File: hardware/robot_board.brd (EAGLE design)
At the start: 95.2 x 76.1 mm, 147 parts, among them J1 POWER_JACKPTH, Q1 DMP2035U, Q2 DMP2035U, Q3 DMP2035U-7, Q4 DMP2035U-7, U1 FT232RL-BASICSSOP, U11 LM393, U12 LM393, U16 LM393, U17 ATMEGA325PA, U2 SIA907EDJT, U3 MIC5219, U4 HC_05, U5 SIA907EDJT, U6 SIA907EDJT, U7 TLV70233, Y1 16MHz

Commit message: updated routing
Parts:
- removed D24: POWER, SparkFun-LED:LED-1206
- added C8: .1uF, resistor:C1206
- added C9: 1uF, resistor:C1206
- added D34: POWER, SparkFun-LED:LED-1206
- added R63: 1K, resistor:R1206
- added U$2: POT, r_cubed:POT
- D23: value 2.1V -> 2.4V; device diode:SOD80C -> SparkFun-DiscreteSemi:SOT23-3
- R24: value 12K -> 12K 1%
- R26: value 7.68K -> 7.68K 1%
- R27, R28, R45, R46: value 10K -> 10K 1%
- R29, R31: value 15K -> 15K 1%
- R58: value 300K -> 300K 1%
- moved D32 13.7 mm to (40.1, 15.5), turned to 270 degrees
- moved R57 7.85 mm to (34.3, 10.4), turned to 90 degrees
- moved Q4 7.60 mm to (88.8, 24.4), turned to 180 degrees
- moved R59 7.08 mm to (44.7, 16.0), turned to 0 degrees
- moved R54 3.64 mm to (44.2, 12.7)
- moved R34 2.86 mm to (85.2, 22.2), turned to 270 degrees
- moved R27 2.80 mm to (85.8, 34.2), turned to 270 degrees
- moved D30 2.54 mm to (2.29, 23.6)
- moved POWER 2.54 mm to (92.7, 15.5)
- moved R51 2.29 mm to (2.29, 18.3)
- moved Q3 2.09 mm to (86.1, 42.9)
- moved C2 2.05 mm to (11.9, 12.2)
- moved C1 1.78 mm to (11.9, 17.8)
- moved Y1 1.78 mm to (8.38, 16.0)
- moved R25 1.78 mm to (83.1, 44.7)
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- renumbered S1 to RESET, U$4 to U9, U$5 to U10, U$6 to U8
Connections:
- new net N$13: R61.1, R62.2, U4.2
- new net N$15: U$1.5, U$2.2
- net 2.1V: now also D23.3; no longer D23.C
- net 3V3: now also C9.1
- net 5V: now also R57.1, U$2.1; no longer U$1.5
- net 5V_UC: now also C8.1
- net BT_RX: now also R61.2; no longer U4.2
- net BT_TX: now also U4.1; no longer R61.1, R62.2
- net DTR: now also R63.1; no longer U1.2
- net GND: now also C8.2, C9.2, D23.1, U$2.3, U1.26; no longer D23.A, R57.1
- net N$10: now also D34.C; no longer D24.A
- net N$11: now also D34.A; no longer D24.C
- net N$14: now also R63.2, U1.2; no longer R61.2, U4.1
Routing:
- net 2.1V: track 87.3 -> 71.8 mm
- net N$15: track 0.00 -> 12.7 mm
- net N$11: track 4.35 -> 13.6 mm, vias 0 -> 2
- net AREF: track 3.91 -> 13.1 mm
- net N$13: track 0.00 -> 7.05 mm, vias 0 -> 1
- net GND: track 301.4 -> 308.4 mm, vias 28 -> 32
- net D1: track 18.7 -> 24.7 mm
- net DTR: track 10.1 -> 4.66 mm, vias 2 -> 0
- net 3V3_OUT: track 26.5 -> 30.8 mm
- net AREF_IN: track 40.7 -> 44.6 mm, vias 4 -> 2
- net BT_RX: track 105.6 -> 101.8 mm, vias 5 -> 8
- net N$10: track 15.3 -> 18.8 mm
- net N$45: track 14.9 -> 18.3 mm
- net 3V3: track 241.7 -> 238.4 mm, vias 10 -> 12
- net N$14: track 6.09 -> 9.37 mm, vias 1 -> 2
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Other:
- board text added: "0"
- board text added: "1"
- board text added: "10"
- board text added: "11"
- board text added: "12"
- board text added: "13"
- board text added: "2"
- board text added: "3"
- board text added: "3.3V"
- board text added: "4"
- board text added: "5"
- board text added: "5V"
- board text added: "6"
- board text added: "7"
- board text added: "8"
- board text added: "9"
- board text added: "AREF"
- board text added: "Analog"
- board text added: "Digital"
- board text added: "GND"
- board text added: "IR"
- board text added: "ISP"
- board text added: "LED0"
- board text added: "LED1"
- board text added: "OFF"
- board text added: "ON"
- board text added: "PWR"
- board text added: "RESET"
- board text added: "SCL"
- board text added: "SDA"
- board text added: "SW1"
- board text added: "Vin"
- board text added: "v0.1"

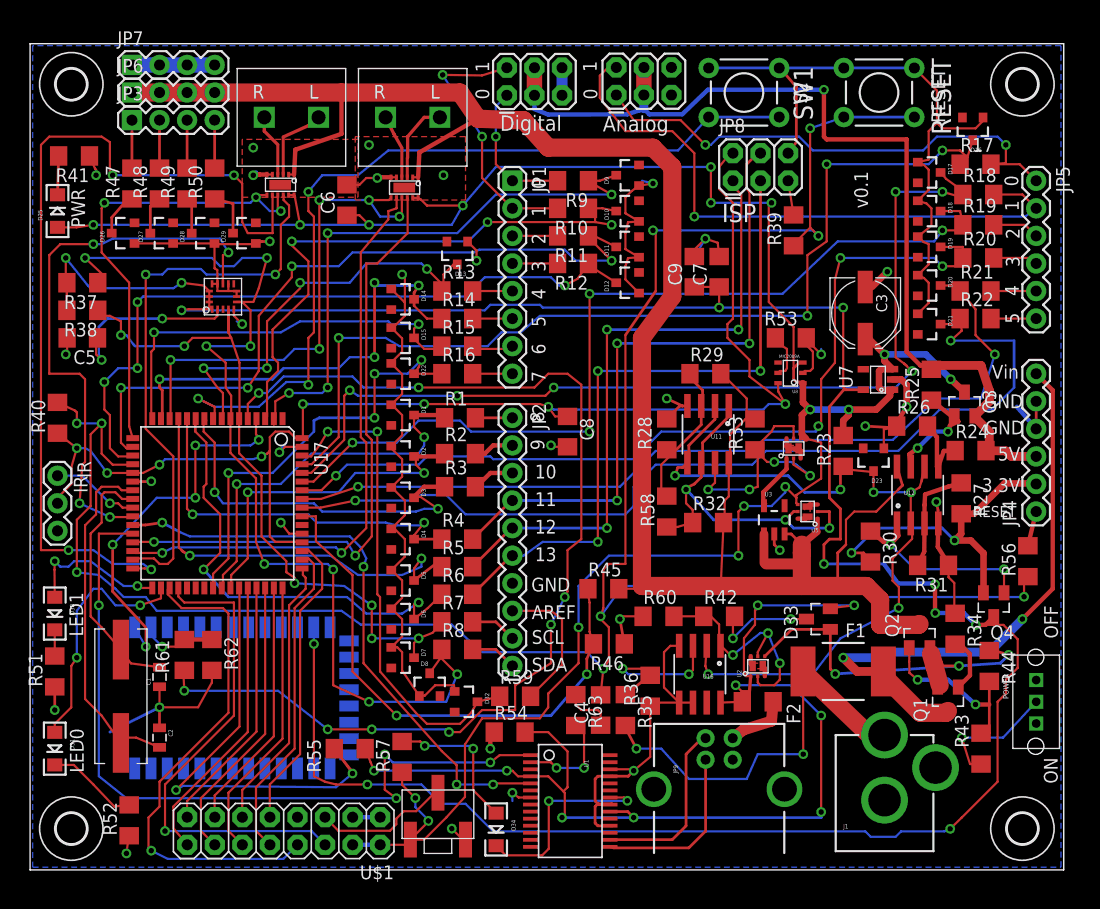
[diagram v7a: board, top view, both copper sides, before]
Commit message: fix analog pin ordering error
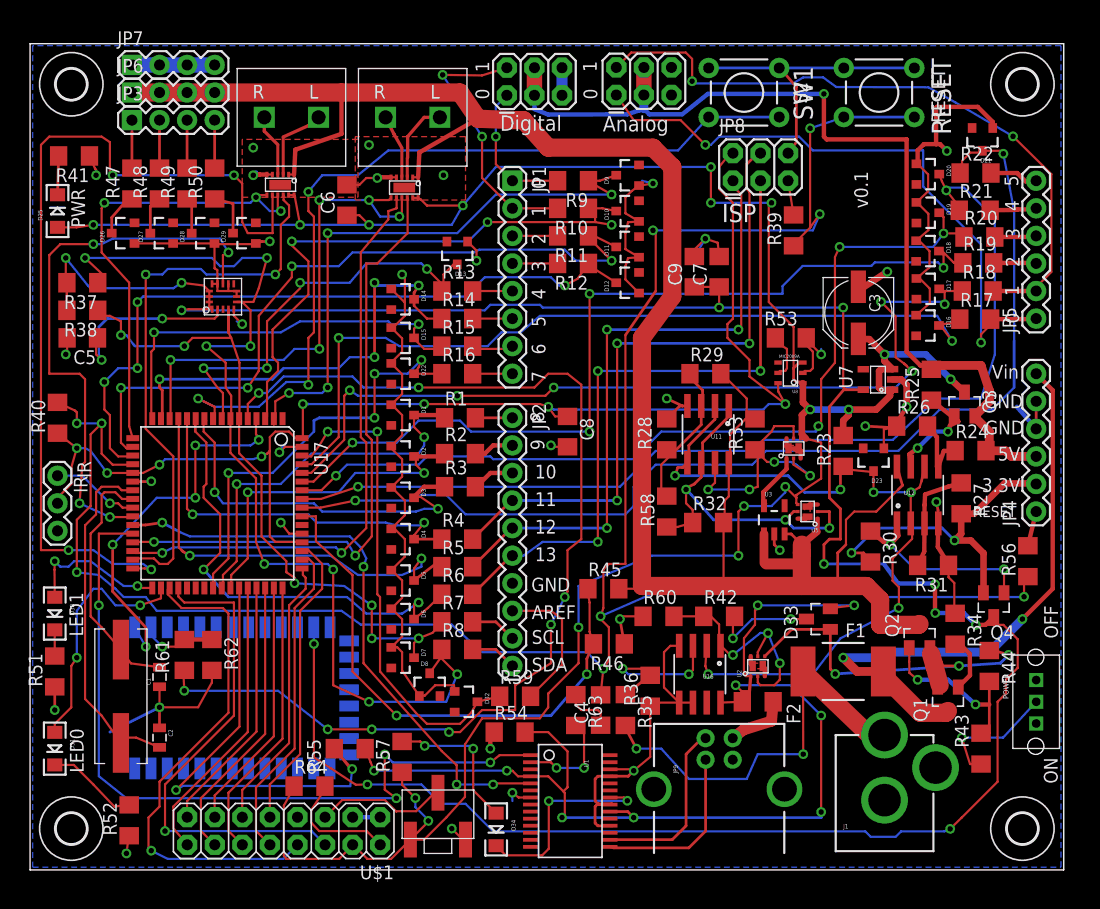
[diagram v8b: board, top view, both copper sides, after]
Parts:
- added R64: 10, resistor:R1206
- moved D16 18.6 mm to (82.7, 50.2), turned to 270 degrees
- moved D21 17.8 mm to (87.8, 67.4), turned to 180 degrees
- moved R17 14.3 mm to (87.1, 50.7)
- moved R22 13.4 mm to (87.1, 64.2)
- moved JP5 12.7 mm to (92.7, 50.8), turned to 90 degrees
- moved D17 10.7 mm to (82.7, 53.5)
- moved D20 10.3 mm to (82.7, 64.1)
- moved R18 8.89 mm to (87.3, 53.3)
- moved R21 7.44 mm to (87.0, 60.8)
- moved D18 3.69 mm to (82.7, 57.0)
- moved R19 3.51 mm to (87.4, 55.9)
- moved D19 3.15 mm to (82.7, 60.6)
- moved R20 1.93 mm to (87.5, 58.3)
- moved C3 0.64 mm to (76.3, 51.3)
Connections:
- new net N$16: R64.2, U$1.2
- net 5V: now also R64.1; no longer U$1.2
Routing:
- net 5V: track 220.9 -> 235.7 mm
- net A4_IN: track 79.3 -> 92.4 mm
- net A5_IN: track 87.2 -> 99.9 mm
- net A0_IN: track 89.2 -> 76.7 mm, vias 4 -> 2
- net N$16: track 0.00 -> 10.9 mm
- net A0: track 47.6 -> 58.1 mm
- net A1_IN: track 90.7 -> 80.6 mm
- net A1: track 57.0 -> 65.2 mm, vias 1 -> 2
- net A2_IN: track 83.1 -> 80.8 mm
- net 3V3: track 238.4 -> 237.3 mm
- net 5V_OUT: track 92.8 -> 92.1 mm
- net RESET: track 205.4 -> 205.9 mm
- net GND: track 308.4 -> 307.9 mm, vias 32 -> 33
